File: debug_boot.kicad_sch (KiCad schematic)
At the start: 11 parts, among them J1 Conn_ARM_JTAG_SWD_10, J2 61300311121, J3 61300311121, J4 61300511121, J5 61300311121

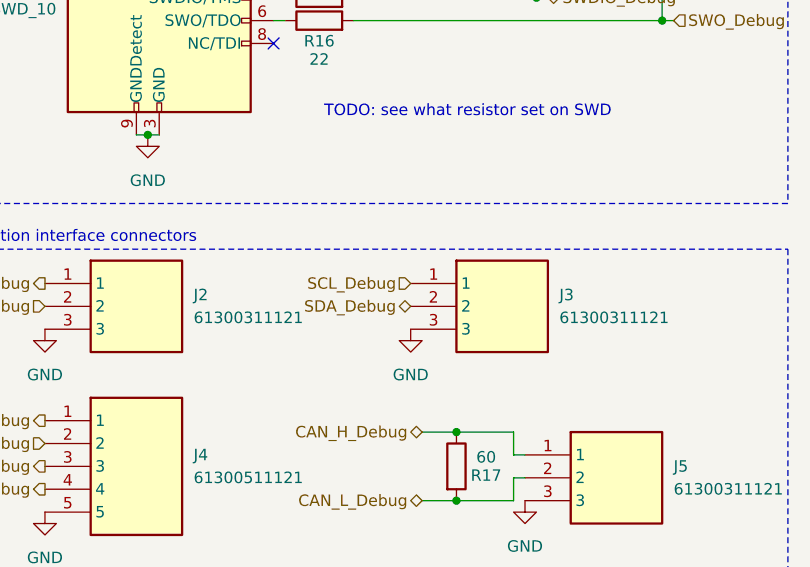
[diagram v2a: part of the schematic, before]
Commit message: Use I2C for slave MCU for bootloader
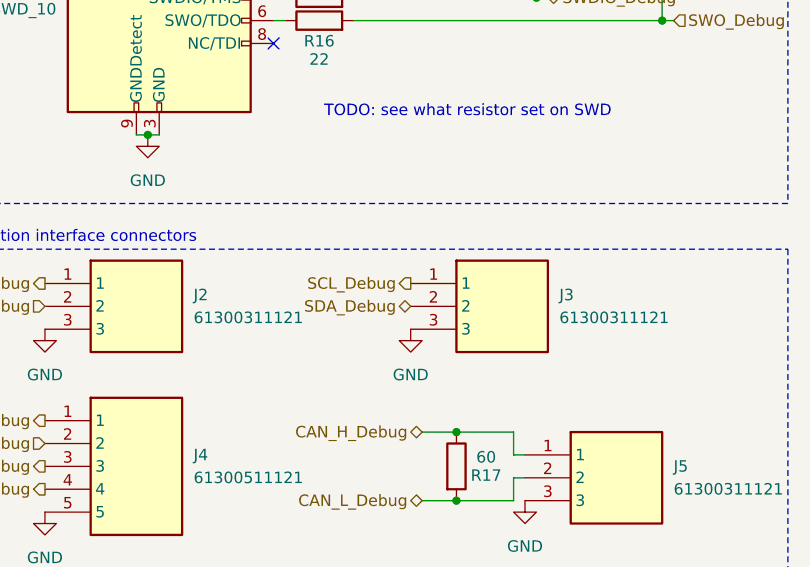
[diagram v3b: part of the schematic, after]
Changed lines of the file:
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@@
 	)
 	(hierarchical_label "SCL_Debug"
-		(shape input)
+		(shape output)
 		(at 160.02 101.6 180)
 		(effects

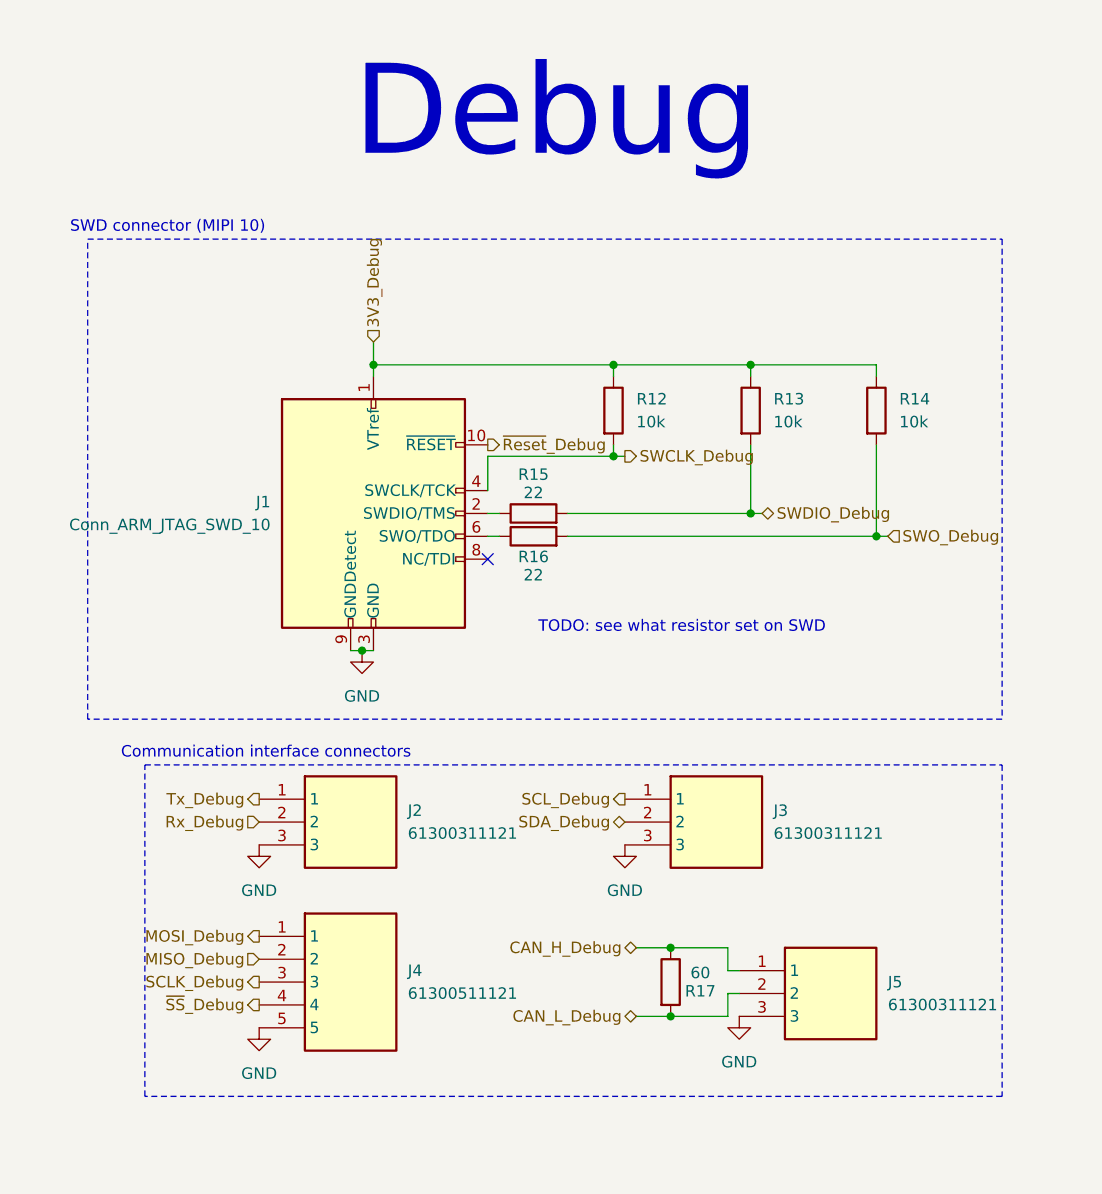
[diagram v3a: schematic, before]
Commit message: Update schematic to Kicad 10
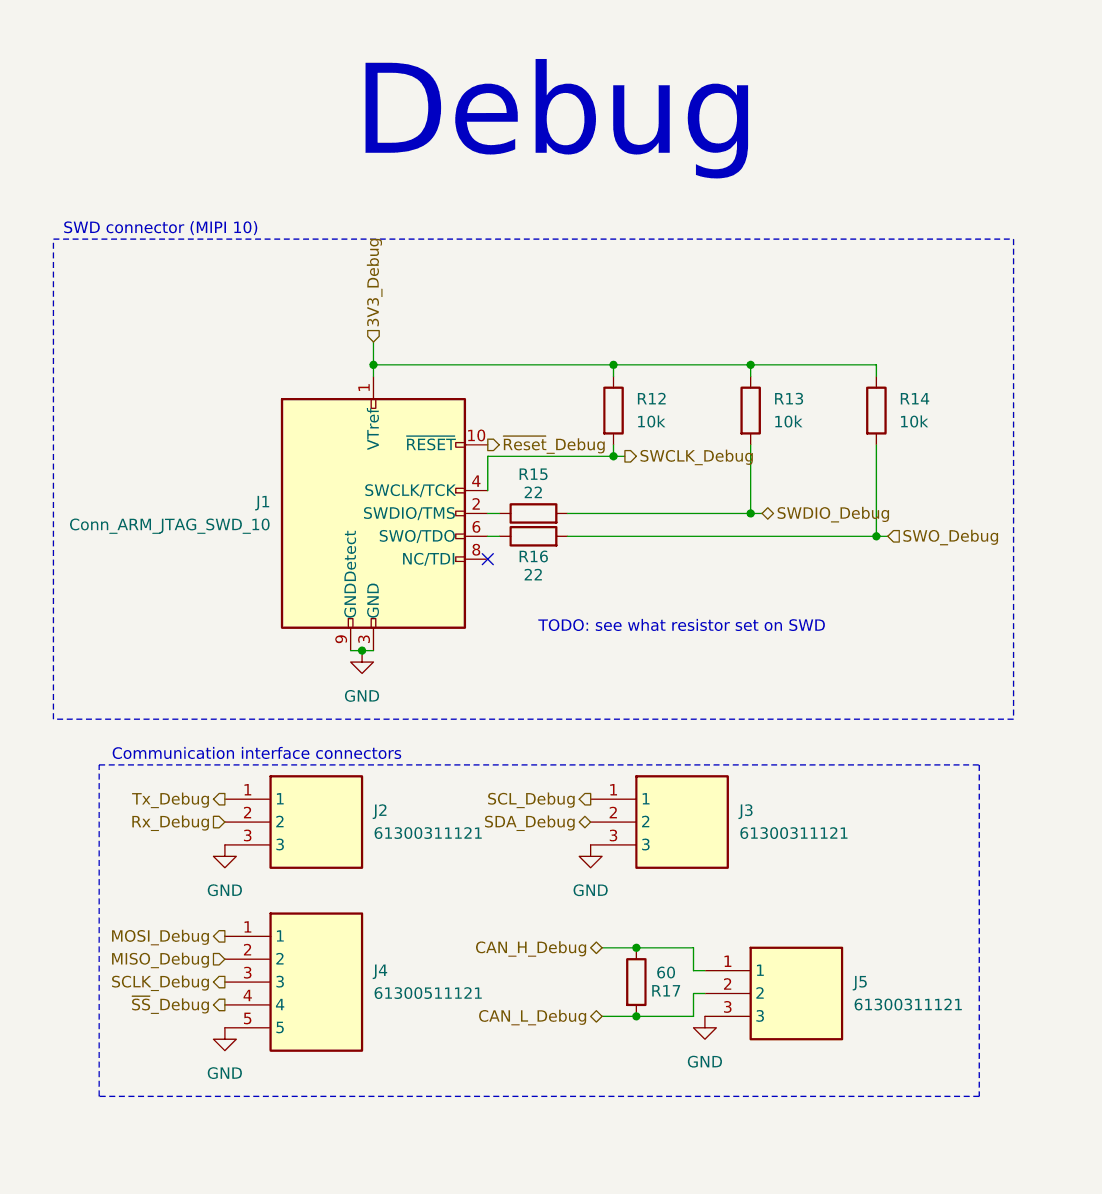
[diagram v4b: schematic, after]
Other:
- moved on the sheet: J2, J3, J4, J5, R17

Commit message: Add tests points with 5015 footprint for practicity
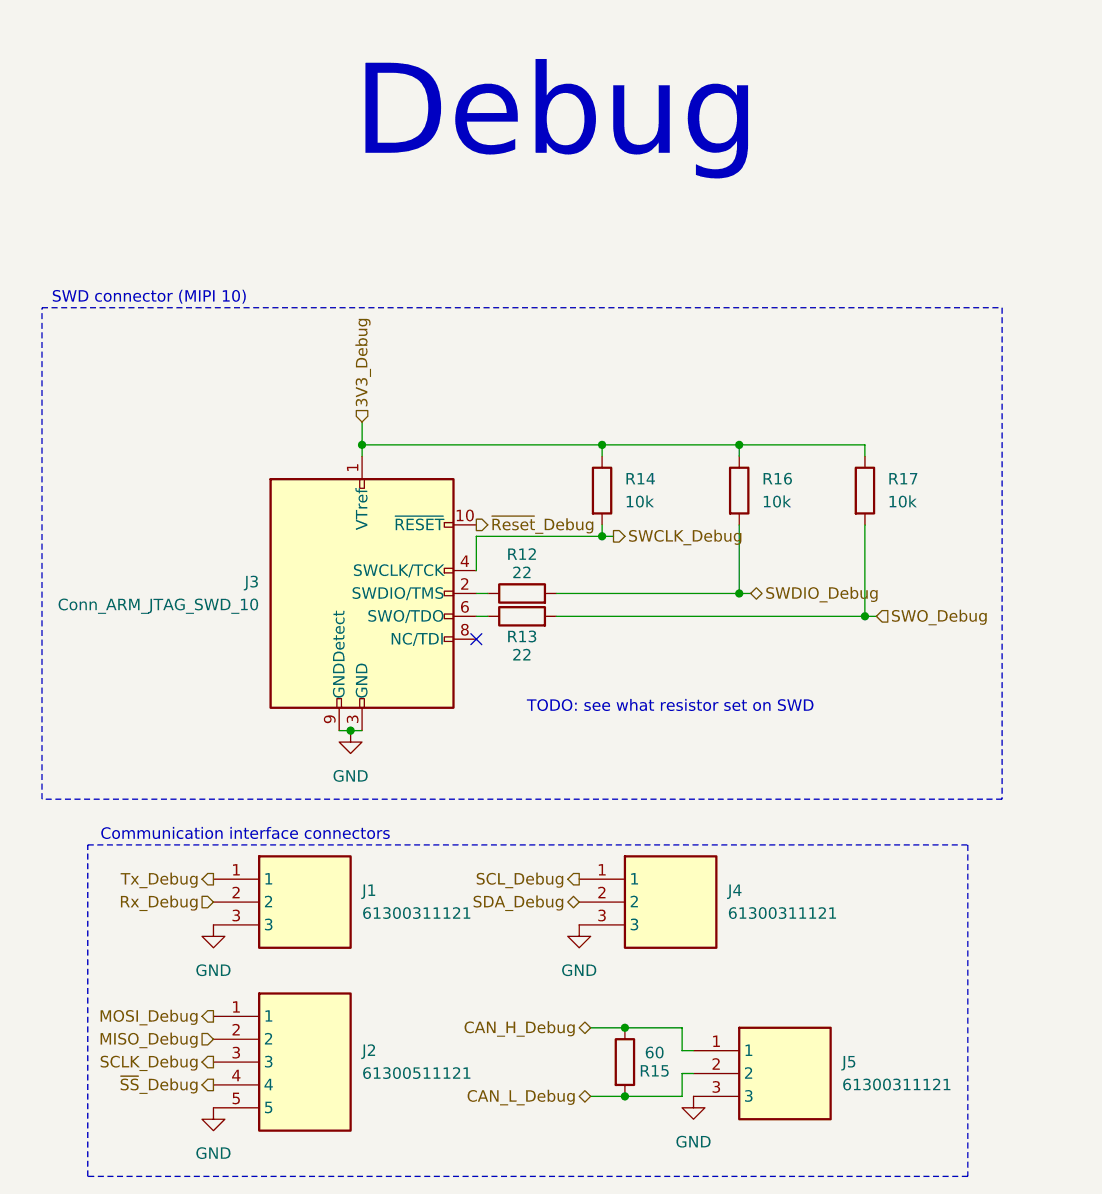
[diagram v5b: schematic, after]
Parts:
- renumbered J2 to J1, J4 to J2, J1 to J3, J3 to J4, R15 to R12, R16 to R13, R12 to R14, R17 to R15, R13 to R16, R14 to R17
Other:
- moved on the sheet: J1, J2, J3, J4, J5, R12, R13, R14, R15, R16, R17

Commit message: Add pull ups resistors for I2C bus and reformat some schematic files
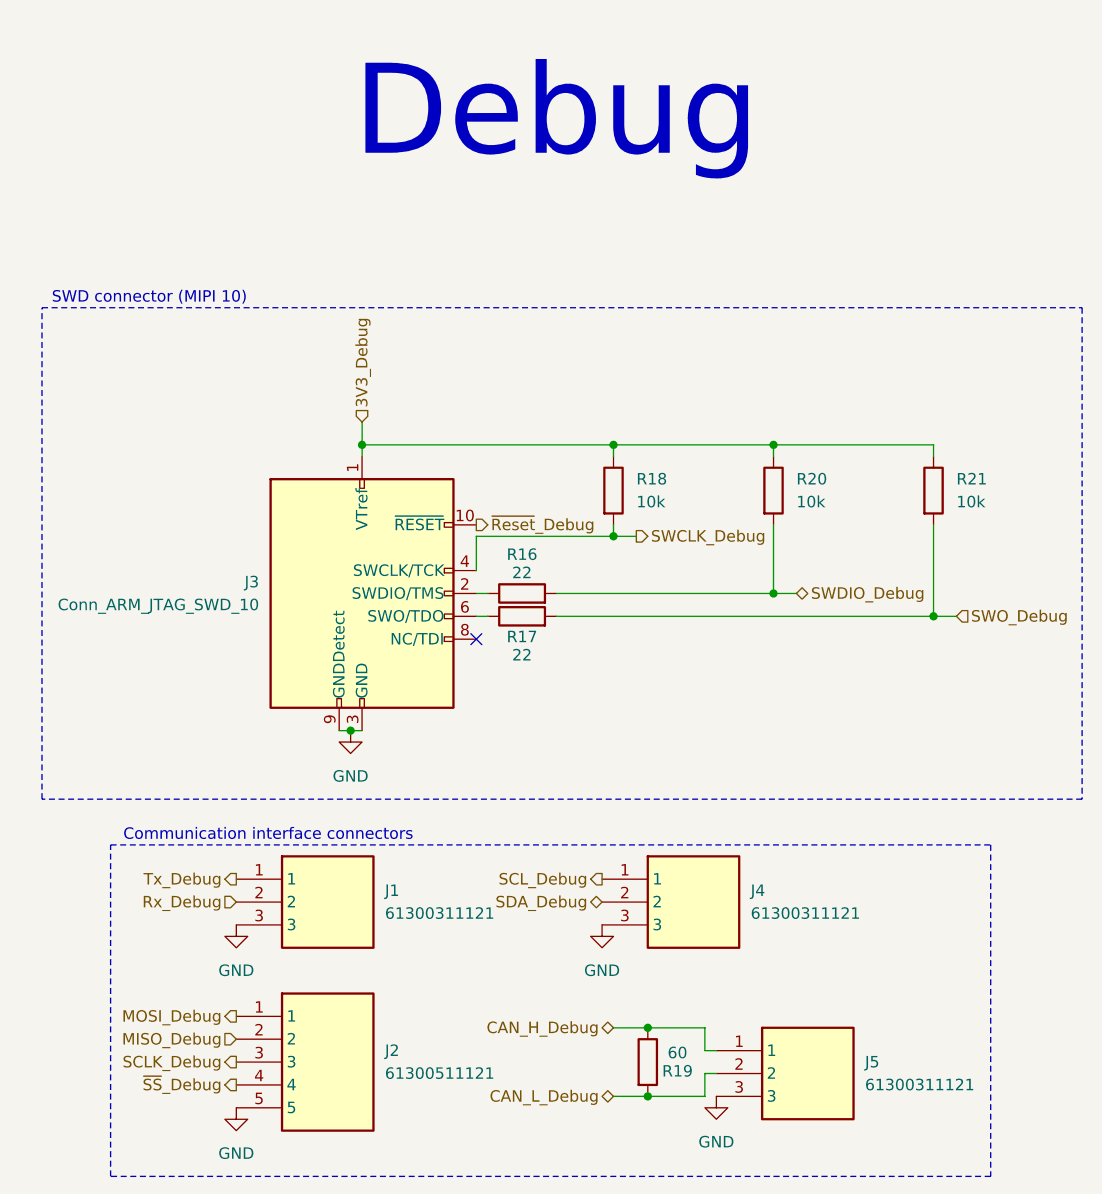
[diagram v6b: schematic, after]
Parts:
- renumbered R12 to R16, R13 to R17, R14 to R18, R15 to R19, R16 to R20, R17 to R21
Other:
- note removed: "TODO: see what resistor set on SWD"
- moved on the sheet: J1, J2, J4, J5, R18, R19, R20, R21

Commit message: Complete all references for components
Modifgy Y1 and Y2 capacitors footprint from 0603 to 0402
Modify footprint of SWD connector
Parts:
- J3: footprint Connector_PinHeader_1.27mm:PinHeader_2x05_P1.27mm_Vertical_SMD -> weather-station-poc-fp:FTSH10501LDVK; Manufacturer_Name (none) -> Samtec; Manufacturer_Part_Number (none) -> FTSH-105-01-L-DV-K
- R16, R17: Manufacturer_Name (none) -> Wurth Elektronik; Manufacturer_Part_Number (none) -> 560112116043
- R18, R20, R21: Manufacturer_Name (none) -> Wurth Elektronik; Manufacturer_Part_Number (none) -> 560112116005
- R19: Manufacturer_Name (none) -> Vishay; Manufacturer_Part_Number (none) -> CRCW060317K4FKEC
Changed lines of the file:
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@@
 			)
 		)
-		(property "Datasheet" ""
+		(property "Datasheet" "https://www.vishay.com/docs/20035/dcrcwe3.pdf"
 			(at 162.56 130.81 0)
 			(hide yes)
@@
 		)
 		(property "Description" "Resistor"
+			(at 162.56 130.81 0)
+			(hide yes)
+			(show_name no)
+			(do_not_autoplace no)
+			(effects
+				(font
+					(size 1.27 1.27)
+				)
+			)
+		)
+		(property "Manufacturer_Name" "Vishay"
+			(at 162.56 130.81 0)
+			(hide yes)
+			(show_name no)
+			(do_not_autoplace no)
+			(effects
+				(font
+					(size 1.27 1.27)
+				)
+			)
+		)
+		(property "Manufacturer_Part_Number" "CRCW060317K4FKEC"
 			(at 162.56 130.81 0)
 			(hide yes)
@@
 			)
 		)
-		(property "Datasheet" ""
+		(property "Datasheet" "https://www.we-online.com/components/products/datasheet/560112116043.pdf"
 			(at 148.59 81.28 0)
 			(hide yes)
@@
 		(property "Description" "Resistor"
 			(at 148.59 81.28 0)
+			(hide yes)
+			(show_name no)
+			(do_not_autoplace no)
+			(effects
+				(font
+					(size 1.27 1.27)
+				)
+			)
+		)
+		(property "Manufacturer_Name" "Wurth Elektronik"
+			(at 148.59 81.28 90)
+			(hide yes)
+			(show_name no)
+			(do_not_autoplace no)
+			(effects
+				(font
+					(size 1.27 1.27)
+				)
+			)
+		)
+		(property "Manufacturer_Part_Number" "560112116043"
+			(at 148.59 81.28 90)
 			(hide yes)
 			(show_name no)
@@
 			)
 		)
-		(property "Datasheet" ""
+		(property "Datasheet" "https://www.we-online.com/components/products/datasheet/560112116005.pdf"
 			(at 176.53 67.31 0)
 			(hide yes)
@@
 		)
 		(property "Description" "Resistor"
+			(at 176.53 67.31 0)
+			(hide yes)
+			(show_name no)
+			(do_not_autoplace no)
+			(effects
+				(font
+					(size 1.27 1.27)
+				)
+			)
+		)
+		(property "Manufacturer_Name" "Wurth Elektronik"
+			(at 176.53 67.31 0)
+			(hide yes)
+			(show_name no)
+			(do_not_autoplace no)
+			(effects
+				(font
+					(size 1.27 1.27)
+				)
+			)
+		)
+		(property "Manufacturer_Part_Number" "560112116005"
 			(at 176.53 67.31 0)
 			(hide yes)
@@
 			)
 		)
-		(property "Datasheet" ""
+		(property "Datasheet" "https://www.we-online.com/components/products/datasheet/560112116043.pdf"
 			(at 148.59 78.74 0)
 			(hide yes)
@@
 		(property "Description" "Resistor"
 			(at 148.59 78.74 0)
+			(hide yes)
+			(show_name no)
+			(do_not_autoplace no)
+			(effects
+				(font
+					(size 1.27 1.27)
+				)
+			)
+		)
+		(property "Manufacturer_Name" "Wurth Elektronik"
+			(at 148.59 78.74 90)
+			(hide yes)
+			(show_name no)
+			(do_not_autoplace no)
+			(effects
+				(font
+					(size 1.27 1.27)
+				)
+			)
+		)
+		(property "Manufacturer_Part_Number" "560112116043"
+			(at 148.59 78.74 90)
 			(hide yes)
 			(show_name no)
@@
 			)
 		)
-		(property "Datasheet" ""
+		(property "Datasheet" "https://www.we-online.com/components/products/datasheet/560112116005.pdf"
 			(at 158.75 67.31 0)
 			(hide yes)
@@
 		)
 		(property "Description" "Resistor"
+			(at 158.75 67.31 0)
+			(hide yes)
+			(show_name no)
+			(do_not_autoplace no)
+			(effects
+				(font
+					(size 1.27 1.27)
+				)
+			)
+		)
+		(property "Manufacturer_Name" "Wurth Elektronik"
+			(at 158.75 67.31 0)
+			(hide yes)
+			(show_name no)
+			(do_not_autoplace no)
+			(effects
+				(font
+					(size 1.27 1.27)
+				)
+			)
+		)
+		(property "Manufacturer_Part_Number" "560112116005"
 			(at 158.75 67.31 0)
 			(hide yes)
@@
 			)
 		)
-		(property "Footprint" "Connector_PinHeader_1.27mm:PinHeader_2x05_P1.27mm_Vertical_SMD"
+		(property "Footprint" "weather-station-poc-fp:FTSH10501LDVK"
 			(at 130.81 78.74 0)
 			(hide yes)
@@
 		)
 		(property "Description" "Cortex Debug Connector, standard ARM Cortex-M SWD and JTAG interface"
+			(at 130.81 78.74 0)
+			(hide yes)
+			(show_name no)
+			(do_not_autoplace no)
+			(effects
+				(font
+					(size 1.27 1.27)
+				)
+			)
+		)
+		(property "Manufacturer_Name" "Samtec"
+			(at 130.81 78.74 0)
+			(hide yes)
+			(show_name no)
+			(do_not_autoplace no)
+			(effects
+				(font
+					(size 1.27 1.27)
+				)
+			)
+		)
+		(property "Manufacturer_Part_Number" "FTSH-105-01-L-DV-K"
 			(at 130.81 78.74 0)
 			(hide yes)
@@
 			)
 		)
-		(property "Datasheet" ""
+		(property "Datasheet" "https://www.we-online.com/components/products/datasheet/560112116005.pdf"
 			(at 194.31 67.31 0)
 			(hide yes)
@@
 			(at 194.31 67.31 0)
 			(hide yes)
+			(show_name no)
+			(do_not_autoplace no)
+			(effects
+				(font
+					(size 1.27 1.27)
+				)
+			)
+		)
+		(property "Manufacturer_Name" "Wurth Elektronik"
+			(at 194.31 67.31 0)
+			(hide yes)
+			(show_name no)
+			(do_not_autoplace no)
+			(effects
+				(font
+					(size 1.27 1.27)
+				)
+			)
+		)
+		(property "Manufacturer_Part_Number" "560112116005"
+			(at 194.31 67.31 0)
+			(hide yes)

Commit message: End of BOM
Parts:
- R19: value 60 -> 120; Manufacturer_Name Vishay -> Wurth Elektronik; Manufacturer_Part_Number CRCW060317K4FKEC -> 560112116092
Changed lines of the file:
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@@
 			)
 		)
-		(property "Value" "60"
+		(property "Value" "120"
 			(at 165.862 129.794 0)
 			(show_name no)
@@
 			)
 		)
-		(property "Datasheet" "https://www.vishay.com/docs/20035/dcrcwe3.pdf"
+		(property "Datasheet" "https://www.we-online.com/components/products/datasheet/560112116092.pdf"
 			(at 162.56 130.81 0)
 			(hide yes)
@@
 			)
 		)
-		(property "Manufacturer_Name" "Vishay"
+		(property "Manufacturer_Name" "Wurth Elektronik"
 			(at 162.56 130.81 0)
 			(hide yes)
@@
 			)
 		)
-		(property "Manufacturer_Part_Number" "CRCW060317K4FKEC"
+		(property "Manufacturer_Part_Number" "560112116092 "
 			(at 162.56 130.81 0)
 			(hide yes)
